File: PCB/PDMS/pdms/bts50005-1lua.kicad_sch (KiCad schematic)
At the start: 11 parts, among them Q3 BTS500101LUAAUMA1

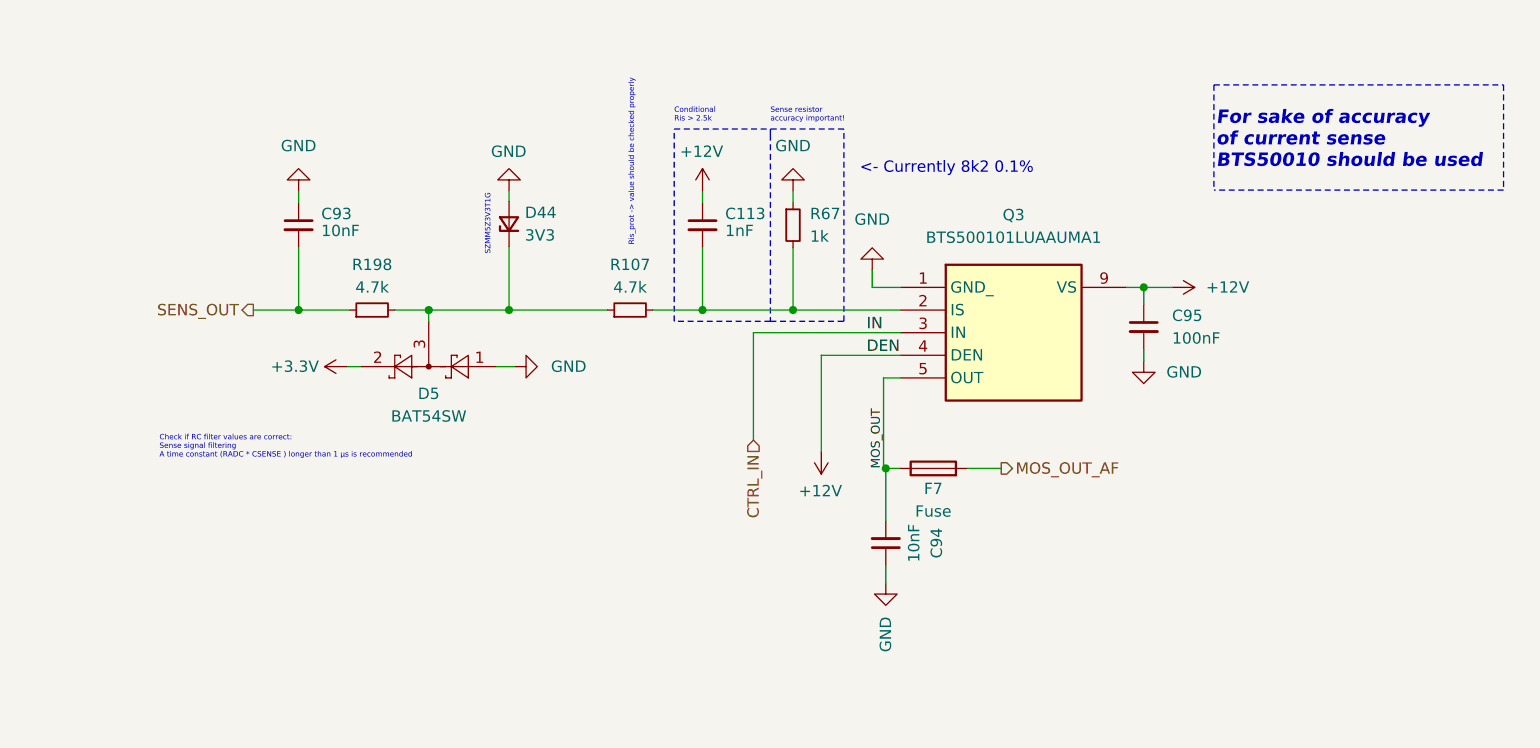
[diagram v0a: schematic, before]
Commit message: Fixed memory and aux routing, fixed decoupling of MCU, fixed hse oscilator layout, fixed BTS500 input capacitors size and thermal, fixed via stiching on output channels, changed LP mos  traces to thiner ones, WIP mp4322 layout repliacte
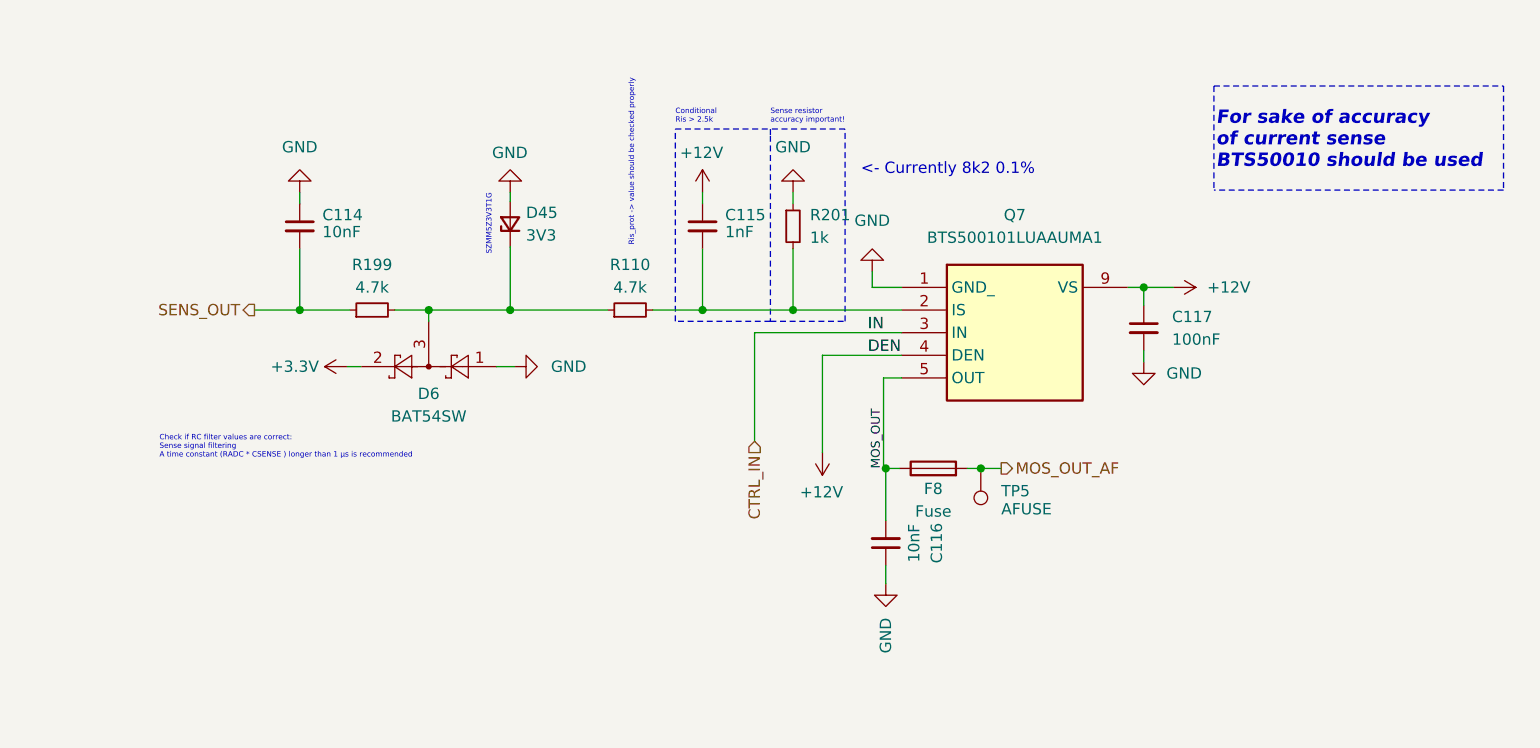
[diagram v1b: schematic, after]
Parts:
- added TP5: AFUSE, TestPoint:TestPoint_Pad_D2.0mm, symbol Connector:TestPoint
- C117: renamed from C95; footprint Capacitor_SMD:C_0402_1005Metric -> Capacitor_SMD:C_0805_2012Metric
- renumbered C93 to C114, C113 to C115, C94 to C116, D44 to D45, D5 to D6, F7 to F8, Q3 to Q7, R107 to R110, R198 to R199, R67 to R201
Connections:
- net MOS_OUT_AF: now also TP5.1

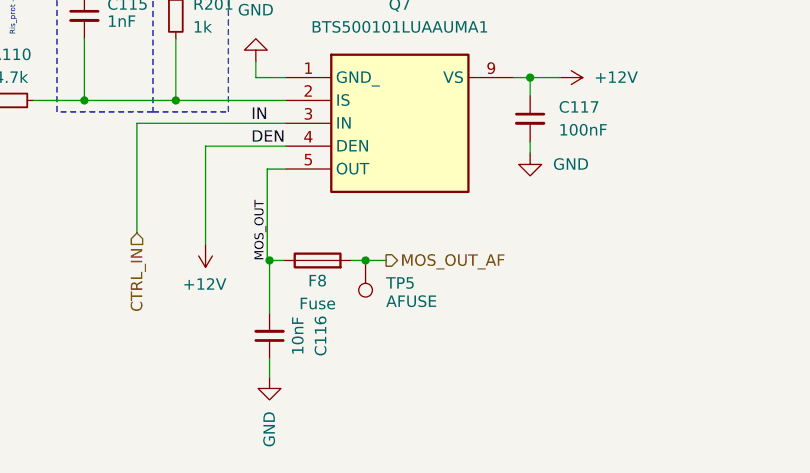
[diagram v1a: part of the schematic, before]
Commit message: PDMS PCB WIP modification mp4322 finished layput, cleared USB-C layout, moved OSC32 for better fit
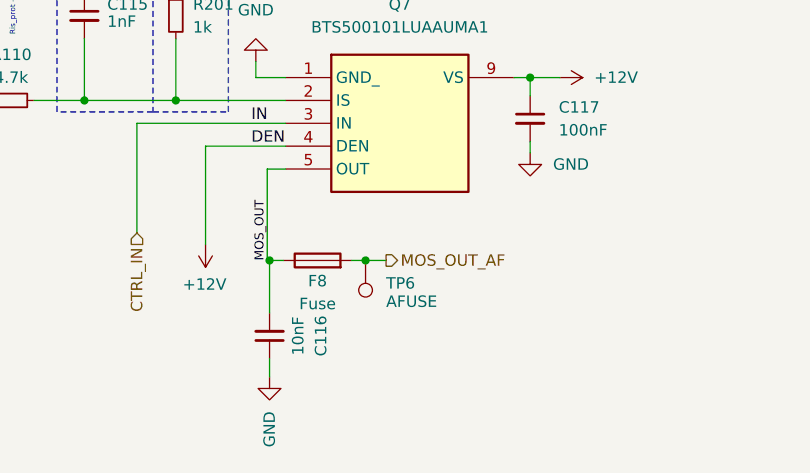
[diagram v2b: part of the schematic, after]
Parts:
- renumbered TP5 to TP6
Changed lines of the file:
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@@
 		(on_board yes)
 		(dnp no)
-		(property "Reference" "TP5"
+		(property "Reference" "TP6"
 			(at 121.666 85.598 0)
 			(effects

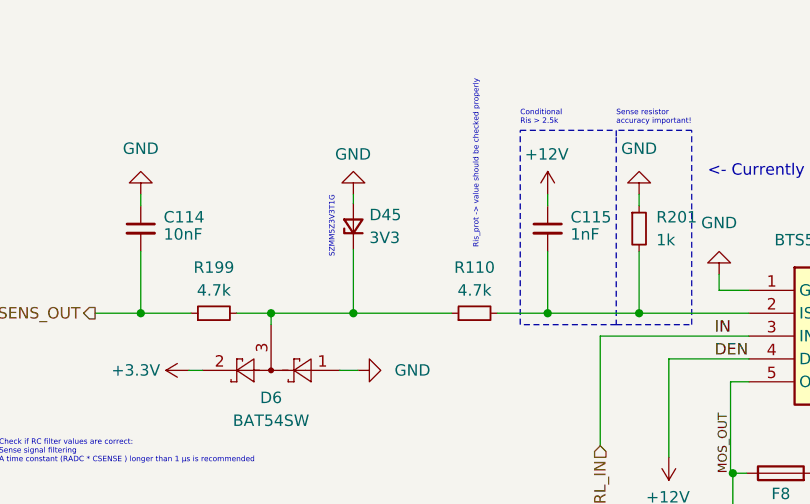
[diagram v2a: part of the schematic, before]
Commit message: PDMS PCB WIP modification - added better input protection and filtering for voltage channels
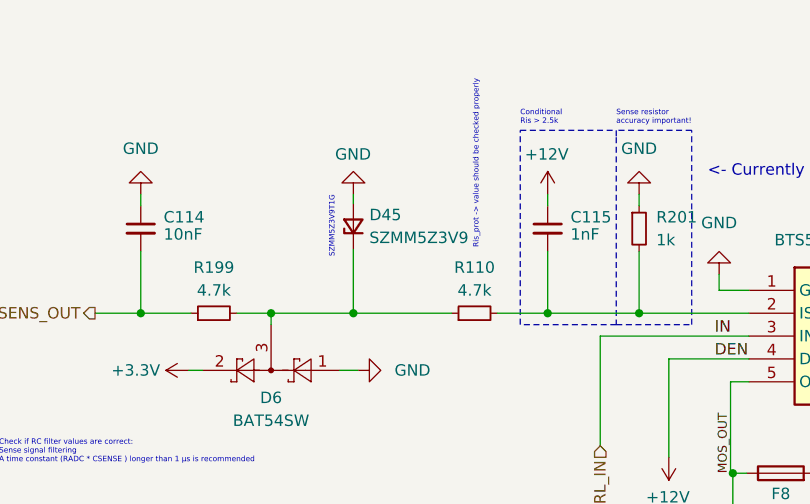
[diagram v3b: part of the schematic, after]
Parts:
- D45: value 3V3 -> SZMM5Z3V9
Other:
- note added: "SZMM5Z3V9T1G"
- note removed: "SZMM5Z3V3T1G"
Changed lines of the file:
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@@
 		)
 	)
-	(text "SZMM5Z3V3T1G "
+	(text "SZMM5Z3V9T1G "
 		(exclude_from_sim no)
 		(at 64.516 59.182 90)
@@
 			)
 		)
-		(property "Value" "3V3"
+		(property "Value" "SZMM5Z3V9"
 			(at 68.326 56.8959 90)
 			(effects

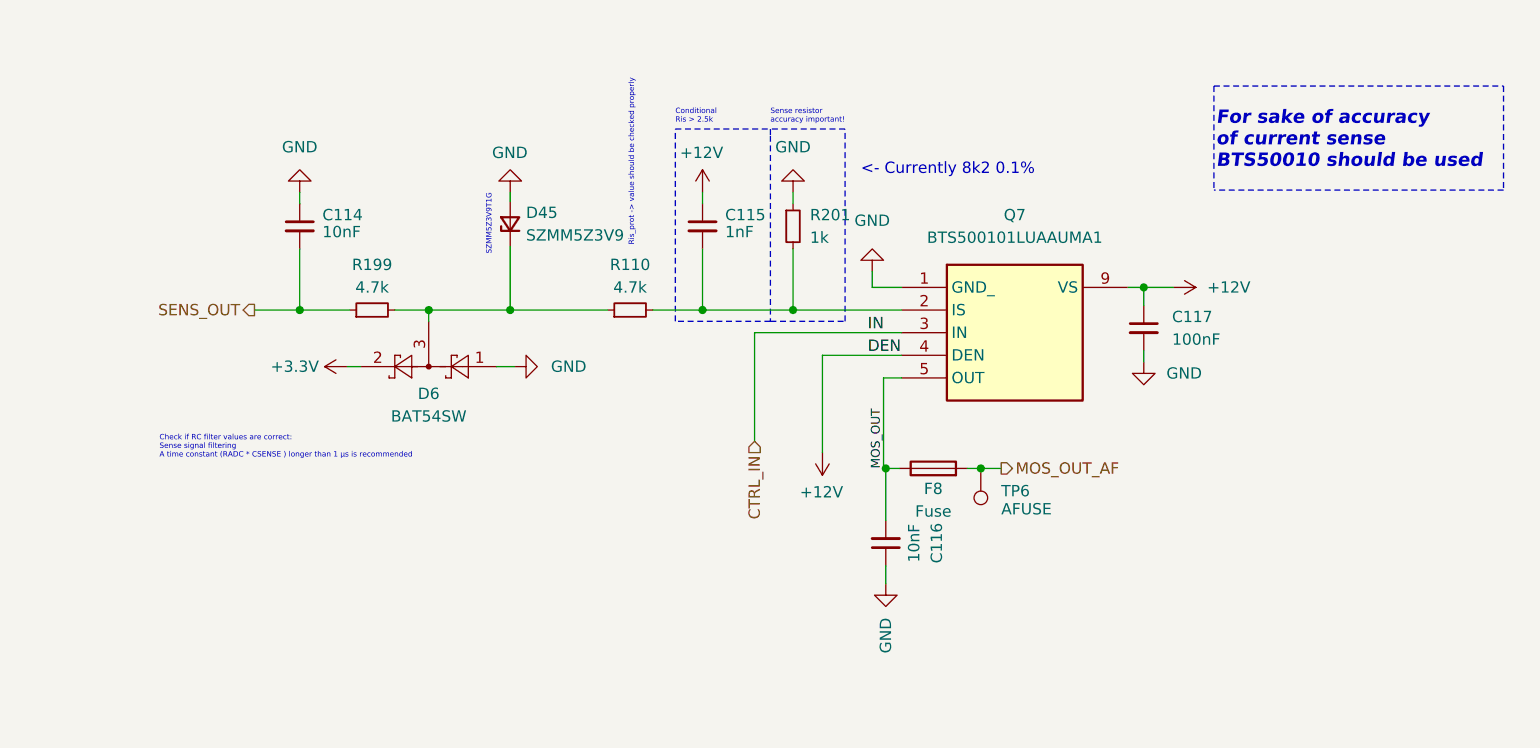
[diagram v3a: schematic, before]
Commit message: Added gerbers of PDMS v4.3, assembly docs, modified DNP parameters
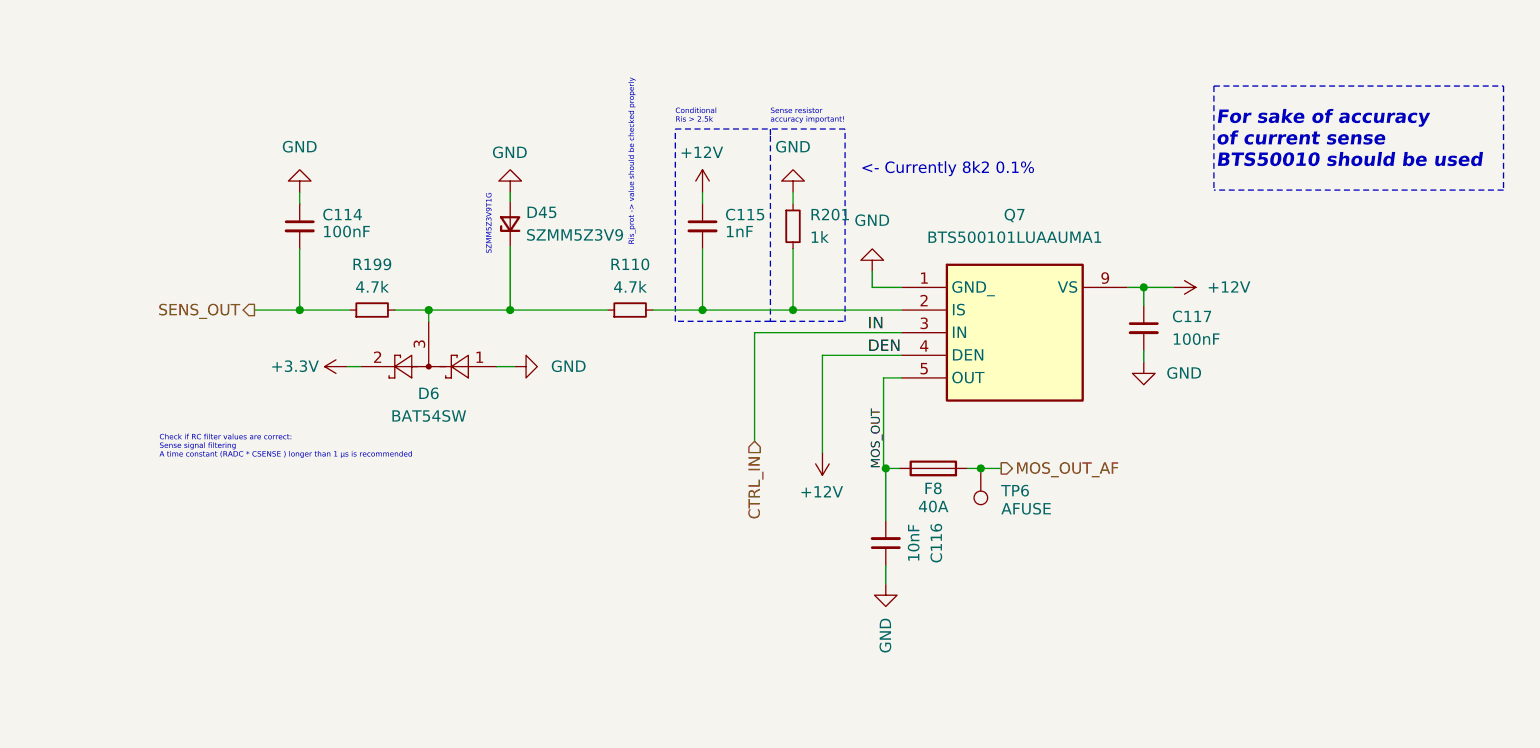
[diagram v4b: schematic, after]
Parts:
- C114: value 10nF -> 100nF
- F8: value Fuse -> 40A
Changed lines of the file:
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@@
 			)
 		)
-		(property "Value" "Fuse"
-			(at 114.046 87.884 90)
+		(property "Value" "40A"
+			(at 114.046 87.376 90)
 			(effects
 				(font
@@
 			)
 		)
-		(property "Value" "10nF"
+		(property "Value" "100nF"
 			(at 45.466 56.515 0)
 			(effects

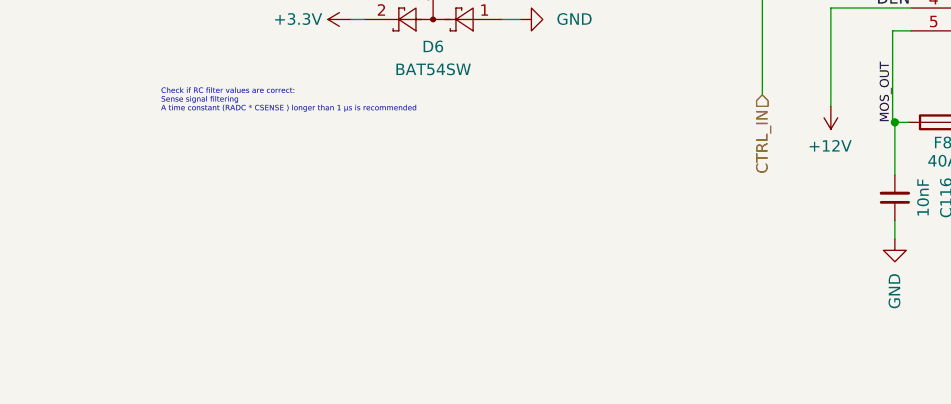
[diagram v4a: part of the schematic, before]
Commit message: Marked changes and notes for future PCB, anti-aliasing filter cacitors soldered on top of vmux divider, DEN should be controlled via IN, so no open-circuit is detected during PWM
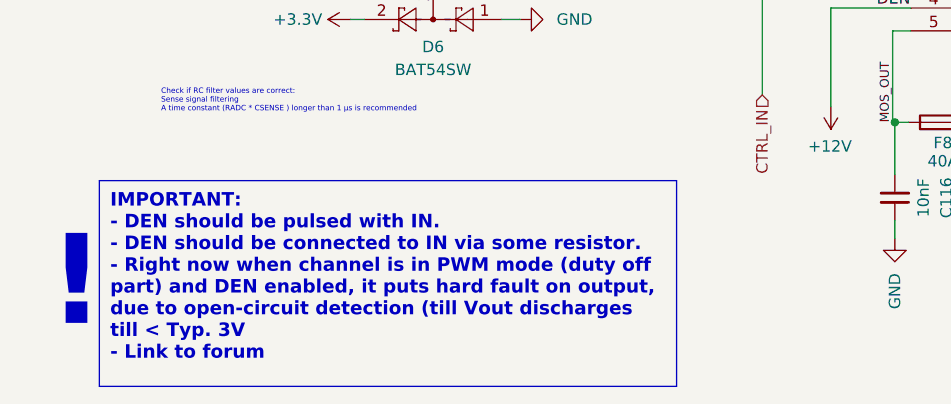
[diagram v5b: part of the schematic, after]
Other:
- note added: "!"
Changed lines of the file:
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@@
+		)
+	)
+	(text_box "IMPORTANT:\n- DEN should be pulsed with IN.\n- DEN should be connected to IN via some resistor.\n- Right now when channel is in PWM mode (duty off part) and DEN enabled, it puts hard fault on output, due to open-circuit detection (till Vout discharges till < Typ. 3V\n- Link to forum"
+		(exclude_from_sim no)
+		(at 20.32 89.535 0)
+		(size 64.135 22.86)
+		(stroke
+			(width 0)
+			(type default)
+			(color 255 0 255 1)
+		)
+		(fill
+			(type none)
+		)
+		(effects
+			(font
+				(size 1.5 1.5)
+				(thickness 0.3)
+				(bold yes)
+				(color 255 0 255 1)
+			)
+			(justify left top)
+			(href "https://community.infineon.com/t5/Smart-Power-Switches/BTS50010-1LUA-Current-Sense/td-p/618180")
 		)
 	)
@@
 		)
 	)
+	(text "!"
+		(exclude_from_sim no)
+		(at 17.78 100.965 0)
+		(effects
+			(font
+				(size 10 10)
+				(thickness 0.6)
+				(bold yes)
+				(color 255 0 255 1)
+			)
+		)
+	)
